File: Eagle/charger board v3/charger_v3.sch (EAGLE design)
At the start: 37 parts, among them IC1 IR2110D, Q2 IRFP240, Q3 MJE13003G

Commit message: benerin opto
benerin opto
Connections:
- removed net N$11: OK1.COL, R1.2
- new net N$9: OK1.A, R1.2
- net 5V: now also OK1.COL; no longer R1.1
- net PWM_SW1: now also R1.1; no longer OK1.A
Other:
- moved on the sheet: R1
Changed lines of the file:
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@@
 <?xml version="1.0" encoding="utf-8"?>
 <!DOCTYPE eagle SYSTEM "eagle.dtd">
-<eagle version="9.6.1">
+<eagle version="9.6.2">
 <drawing>
 <settings>
@@
 <grid distance="0.1" unitdist="inch" unit="inch" style="lines" multiple="1" display="no" altdistance="0.01" altunitdist="inch" altunit="inch"/>
 <layers>
-<layer number="1" name="Top" color="4" fill="1" visible="yes" active="no"/>
-<layer number="2" name="Route2" color="16" fill="1" visible="yes" active="no"/>
-<layer number="3" name="Route3" color="17" fill="1" visible="yes" active="no"/>
-<layer number="4" name="Route4" color="18" fill="1" visible="yes" active="no"/>
-<layer number="5" name="Route5" color="19" fill="1" visible="yes" active="no"/>
-<layer number="6" name="Route6" color="25" fill="1" visible="yes" active="no"/>
-<layer number="7" name="Route7" color="26" fill="1" visible="yes" active="no"/>
-<layer number="8" name="Route8" color="27" fill="1" visible="yes" active="no"/>
-<layer number="9" name="Route9" color="28" fill="1" visible="yes" active="no"/>
-<layer number="10" name="Route10" color="29" fill="1" visible="yes" active="no"/>
-<layer number="11" name="Route11" color="30" fill="1" visible="yes" active="no"/>
-<layer number="12" name="Route12" color="20" fill="1" visible="yes" active="no"/>
-<layer number="13" name="Route13" color="21" fill="1" visible="yes" active="no"/>
-<layer number="14" name="Route14" color="22" fill="1" visible="yes" active="no"/>
-<layer number="15" name="Route15" color="23" fill="1" visible="yes" active="no"/>
-<layer number="16" name="Bottom" color="1" fill="1" visible="yes" active="no"/>
-<layer number="17" name="Pads" color="2" fill="1" visible="yes" active="no"/>
-<layer number="18" name="Vias" color="2" fill="1" visible="yes" active="no"/>
-<layer number="19" name="Unrouted" color="6" fill="1" visible="yes" active="no"/>
-<layer number="20" name="Dimension" color="24" fill="1" visible="yes" active="no"/>
-<layer number="21" name="tPlace" color="7" fill="1" visible="yes" active="no"/>
-<layer number="22" name="bPlace" color="7" fill="1" visible="yes" active="no"/>
-<layer number="23" name="tOrigins" color="15" fill="1" visible="yes" active="no"/>
-<layer number="24" name="bOrigins" color="15" fill="1" visible="yes" active="no"/>
-<layer number="25" name="tNames" color="7" fill="1" visible="yes" active="no"/>
-<layer number="26" name="bNames" color="7" fill="1" visible="yes" active="no"/>
-<layer number="27" name="tValues" color="7" fill="1" visible="yes" active="no"/>
-<layer number="28" name="bValues" color="7" fill="1" visible="yes" active="no"/>
+<layer number="1" name="Top" color="4" fill="1" visible="no" active="no"/>
+<layer number="2" name="Route2" color="16" fill="1" visible="no" active="no"/>
+<layer number="3" name="Route3" color="17" fill="1" visible="no" active="no"/>
+<layer number="4" name="Route4" color="18" fill="1" visible="no" active="no"/>
+<layer number="5" name="Route5" color="19" fill="1" visible="no" active="no"/>
+<layer number="6" name="Route6" color="25" fill="1" visible="no" active="no"/>
+<layer number="7" name="Route7" color="26" fill="1" visible="no" active="no"/>
+<layer number="8" name="Route8" color="27" fill="1" visible="no" active="no"/>
+<layer number="9" name="Route9" color="28" fill="1" visible="no" active="no"/>
+<layer number="10" name="Route10" color="29" fill="1" visible="no" active="no"/>
+<layer number="11" name="Route11" color="30" fill="1" visible="no" active="no"/>
+<layer number="12" name="Route12" color="20" fill="1" visible="no" active="no"/>
+<layer number="13" name="Route13" color="21" fill="1" visible="no" active="no"/>
+<layer number="14" name="Route14" color="22" fill="1" visible="no" active="no"/>
+<layer number="15" name="Route15" color="23" fill="1" visible="no" active="no"/>
+<layer number="16" name="Bottom" color="1" fill="1" visible="no" active="no"/>
+<layer number="17" name="Pads" color="2" fill="1" visible="no" active="no"/>
+<layer number="18" name="Vias" color="2" fill="1" visible="no" active="no"/>
+<layer number="19" name="Unrouted" color="6" fill="1" visible="no" active="no"/>
+<layer number="20" name="Dimension" color="24" fill="1" visible="no" active="no"/>
+<layer number="21" name="tPlace" color="7" fill="1" visible="no" active="no"/>
+<layer number="22" name="bPlace" color="7" fill="1" visible="no" active="no"/>
+<layer number="23" name="tOrigins" color="15" fill="1" visible="no" active="no"/>
+<layer number="24" name="bOrigins" color="15" fill="1" visible="no" active="no"/>
+<layer number="25" name="tNames" color="7" fill="1" visible="no" active="no"/>
+<layer number="26" name="bNames" color="7" fill="1" visible="no" active="no"/>
+<layer number="27" name="tValues" color="7" fill="1" visible="no" active="no"/>
+<layer number="28" name="bValues" color="7" fill="1" visible="no" active="no"/>
 <layer number="29" name="tStop" color="7" fill="3" visible="no" active="no"/>
 <layer number="30" name="bStop" color="7" fill="6" visible="no" active="no"/>
@@
 <layer number="35" name="tGlue" color="7" fill="4" visible="no" active="no"/>
 <layer number="36" name="bGlue" color="7" fill="5" visible="no" active="no"/>
-<layer number="37" name="tTest" color="7" fill="1" visible="yes" active="no"/>
-<layer number="38" name="bTest" color="7" fill="1" visible="yes" active="no"/>
+<layer number="37" name="tTest" color="7" fill="1" visible="no" active="no"/>
+<layer number="38" name="bTest" color="7" fill="1" visible="no" active="no"/>
 <layer number="39" name="tKeepout" color="4" fill="11" visible="no" active="no"/>
 <layer number="40" name="bKeepout" color="1" fill="11" visible="no" active="no"/>
@@
 <layer number="44" name="Drills" color="7" fill="1" visible="no" active="no"/>
 <layer number="45" name="Holes" color="7" fill="1" visible="no" active="no"/>
-<layer number="46" name="Milling" color="3" fill="1" visible="yes" active="no"/>
-<layer number="47" name="Measures" color="7" fill="1" visible="yes" active="no"/>
-<layer number="48" name="Document" color="7" fill="1" visible="yes" active="no"/>
-<layer number="49" name="Reference" color="7" fill="1" visible="yes" active="no"/>
-<layer number="50" name="dxf" color="7" fill="1" visible="yes" active="no"/>
-<layer number="51" name="tDocu" color="7" fill="1" visible="yes" active="no"/>
-<layer number="52" name="bDocu" color="7" fill="1" visible="yes" active="no"/>
-<layer number="53" name="tGND_GNDA" color="7" fill="9" visible="yes" active="no"/>
-<layer number="54" name="bGND_GNDA" color="1" fill="9" visible="yes" active="no"/>
-<layer number="56" name="wert" color="7" fill="1" visible="yes" active="no"/>
-<layer number="57" name="tCAD" color="7" fill="1" visible="yes" active="no"/>
-<layer number="59" name="tCarbon" color="7" fill="1" visible="yes" active="no"/>
-<layer number="60" name="bCarbon" color="7" fill="1" visible="yes" active="no"/>
+<layer number="46" name="Milling" color="3" fill="1" visible="no" active="no"/>
+<layer number="47" name="Measures" color="7" fill="1" visible="no" active="no"/>
+<layer number="48" name="Document" color="7" fill="1" visible="no" active="no"/>
+<layer number="49" name="Reference" color="7" fill="1" visible="no" active="no"/>
+<layer number="50" name="dxf" color="7" fill="1" visible="no" active="no"/>
+<layer number="51" name="tDocu" color="7" fill="1" visible="no" active="no"/>
+<layer number="52" name="bDocu" color="7" fill="1" visible="no" active="no"/>
+<layer number="53" name="tGND_GNDA" color="7" fill="9" visible="no" active="no"/>
+<layer number="54" name="bGND_GNDA" color="1" fill="9" visible="no" active="no"/>
+<layer number="56" name="wert" color="7" fill="1" visible="no" active="no"/>
+<layer number="57" name="tCAD" color="7" fill="1" visible="no" active="no"/>
+<layer number="59" name="tCarbon" color="7" fill="1" visible="no" active="no"/>
+<layer number="60" name="bCarbon" color="7" fill="1" visible="no" active="no"/>
 <layer number="88" name="SimResults" color="9" fill="1" visible="yes" active="yes"/>
 <layer number="89" name="SimProbes" color="9" fill="1" visible="yes" active="yes"/>
@@
 <attribute name="NAME" x="43.815" y="23.495" size="1.778" layer="95"/>
 </instance>
-<instance part="R1" gate="G$1" x="63.5" y="25.4" smashed="yes" rot="R270">
-<attribute name="NAME" x="64.9986" y="29.21" size="1.778" layer="95" rot="R270"/>
-<attribute name="VALUE" x="60.198" y="29.21" size="1.778" layer="96" rot="R270"/>
+<instance part="R1" gate="G$1" x="33.02" y="20.32" smashed="yes">
+<attribute name="NAME" x="29.21" y="21.8186" size="1.778" layer="95"/>
+<attribute name="VALUE" x="29.21" y="17.018" size="1.778" layer="96"/>
 </instance>
 <instance part="R7" gate="G$1" x="50.8" y="7.62" smashed="yes">
@@
 </segment>
 <segment>
-<pinref part="R1" gate="G$1" pin="1"/>
-<wire x1="63.5" y1="30.48" x2="63.5" y2="33.02" width="0.1524" layer="91"/>
-<label x="63.5" y="33.02" size="1.778" layer="95" rot="R90" xref="yes"/>
+<pinref part="OK1" gate="G$1" pin="COL"/>
+<wire x1="58.42" y1="20.32" x2="60.96" y2="20.32" width="0.1524" layer="91"/>
+<label x="60.96" y="20.32" size="1.778" layer="95" xref="yes"/>
 </segment>
 </net>
@@
 </segment>
 <segment>
-<pinref part="OK1" gate="G$1" pin="A"/>
-<wire x1="40.64" y1="20.32" x2="35.56" y2="20.32" width="0.1524" layer="91"/>
-<label x="35.56" y="20.32" size="1.778" layer="95" rot="R180" xref="yes"/>
+<pinref part="R1" gate="G$1" pin="1"/>
+<wire x1="27.94" y1="20.32" x2="25.4" y2="20.32" width="0.1524" layer="91"/>
+<label x="25.4" y="20.32" size="1.778" layer="95" rot="R180" xref="yes"/>
 </segment>
 </net>
@@
 </segment>
 </net>
-<net name="N$11" class="0">
-<segment>
-<pinref part="OK1" gate="G$1" pin="COL"/>
-<wire x1="58.42" y1="20.32" x2="63.5" y2="20.32" width="0.1524" layer="91"/>
+<net name="N$9" class="0">
+<segment>
+<pinref part="OK1" gate="G$1" pin="A"/>
 <pinref part="R1" gate="G$1" pin="2"/>
-</segment>
-</net>
+<wire x1="38.1" y1="20.32" x2="40.64" y2="20.32" width="0.1524" layer="91"/>
+</segment>
+</net>

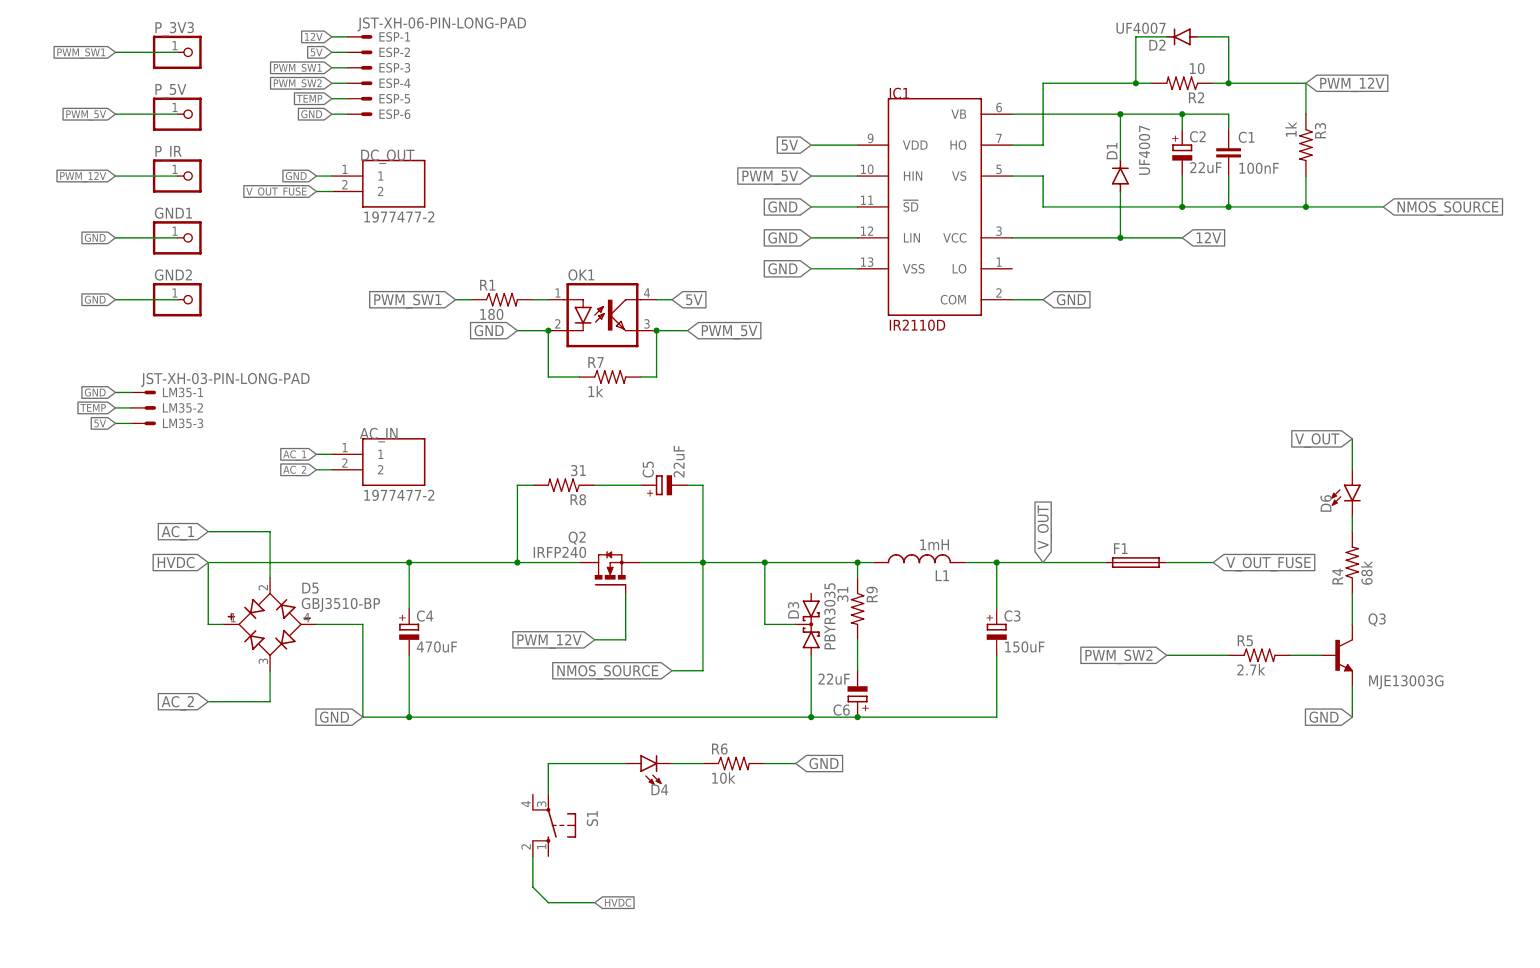
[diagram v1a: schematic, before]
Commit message: update board chg v3
tambah probe buat D-S
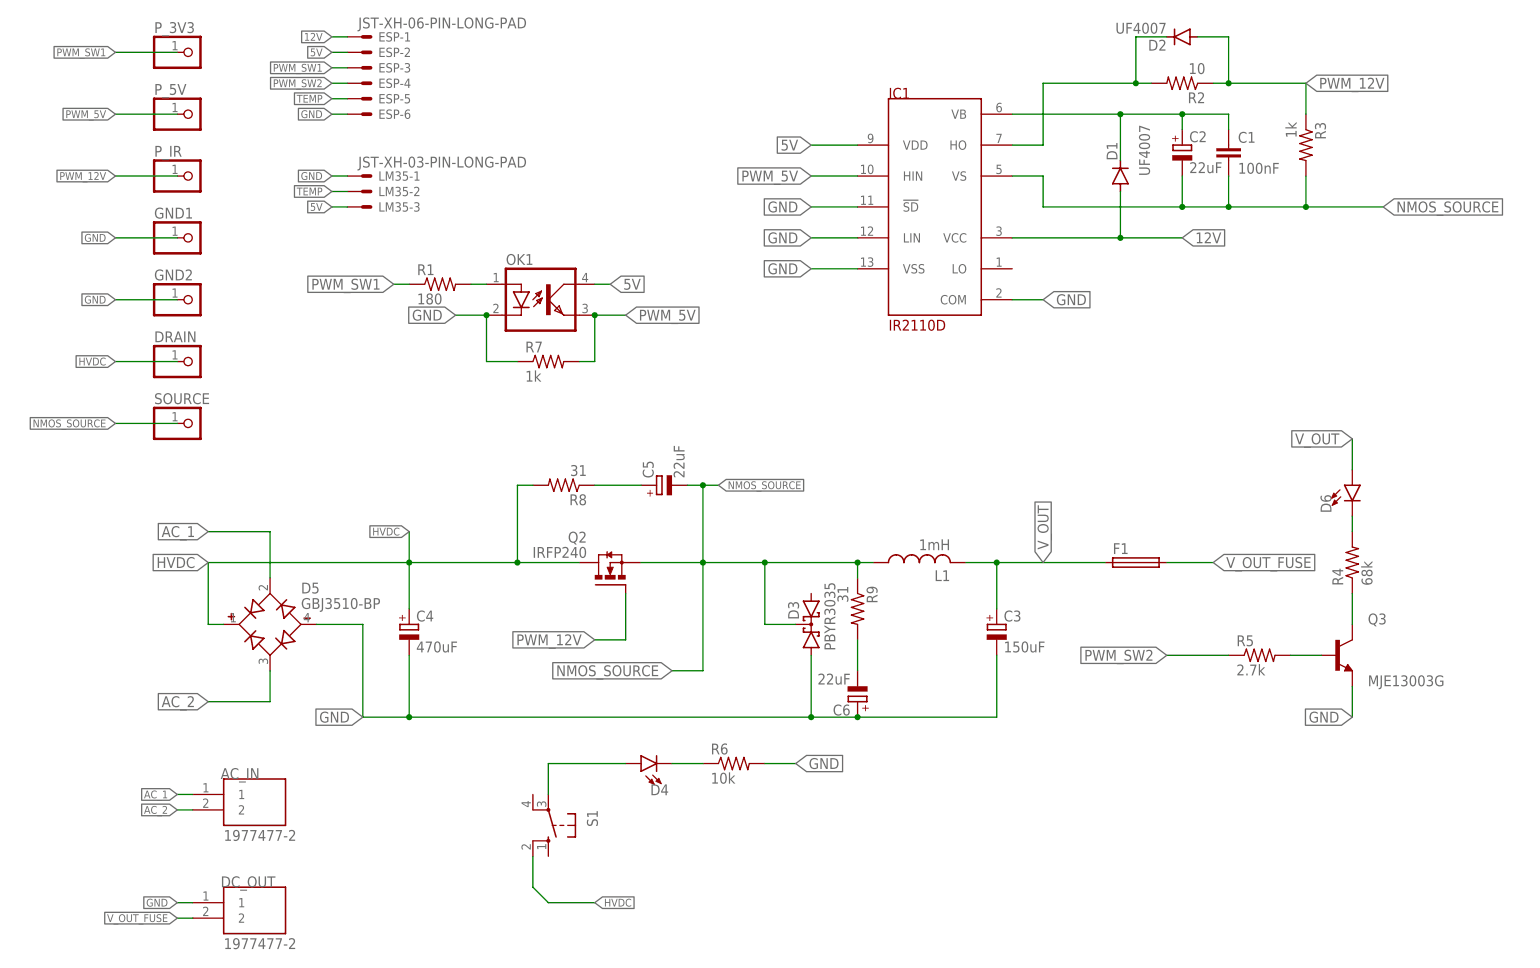
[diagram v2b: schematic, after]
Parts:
- added DRAIN, SOURCE: (no value), pinhead:PINHD-1X1
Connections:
- net HVDC: now also DRAIN.1
- net NMOS_SOURCE: now also SOURCE.1
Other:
- moved on the sheet: AC_IN, DC_OUT, LM35-1, LM35-2, LM35-3, OK1, R1, R7
